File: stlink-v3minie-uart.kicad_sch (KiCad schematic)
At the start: 0 parts

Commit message: schem: add all connectors
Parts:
- added J1: Conn_02x05_Top_Bottom, GLCS:KYOCERA_AVX9159-006, symbol Connector_Generic:Conn_02x05_Top_Bottom
- added J2: Conn_01x04_Pin, Connector_PinHeader_2.54mm:PinHeader_1x04_P2.54mm_Vertical, symbol Connector:Conn_01x04_Pin
- added J3: Conn_01x05, symbol Connector_Generic:Conn_01x05
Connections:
- new net +3V3: J1.10 (Pin_10), J2.1 (Pin_1)
- new net GND: J1.6 (Pin_6), J2.3 (Pin_3)
- new net JTDI: J1.2 (Pin_2), J3.4 (Pin_4)
- new net SWCLK: J1.4 (Pin_4), J3.2 (Pin_2)
- new net SWDIO: J1.3 (Pin_3), J3.3 (Pin_3)
- new net SWO: J1.5 (Pin_5), J3.1 (Pin_1)
- new net VCP_RX: J1.7 (Pin_7), J2.4 (Pin_4)
- new net VCP_TX: J1.8 (Pin_8), J2.2 (Pin_2)
- new net nRST: J1.9 (Pin_9), J3.5 (Pin_5)
- no-connect marks 0 -> 1
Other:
- note added: "Breakout"
- note added: "STLINK-V3MINIE B2B edge connector"
- note added: "UART"

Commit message: schem: assign footprints
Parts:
- J3: footprint (none) -> Connector_PinHeader_2.54mm:PinHeader_1x05_P2.54mm_Horizontal
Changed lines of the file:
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@@
 			)
 		)
-		(property "Footprint" ""
+		(property "Footprint" "Connector_PinHeader_2.54mm:PinHeader_1x05_P2.54mm_Horizontal"
 			(at 105.41 104.14 0)
 			(hide yes)

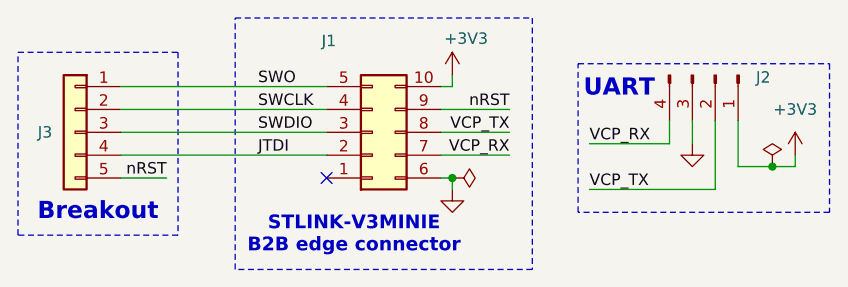
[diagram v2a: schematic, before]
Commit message: schem: renumber
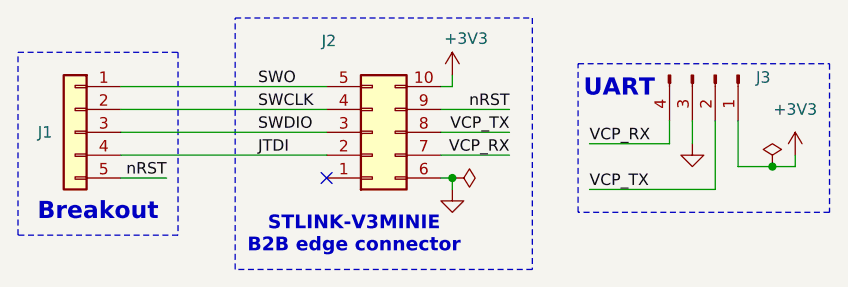
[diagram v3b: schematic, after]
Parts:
- renumbered J3 to J1, J1 to J2, J2 to J3
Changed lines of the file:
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@@
 		(in_pos_files yes)
 		(dnp no)
-		(property "Reference" "J1"
+		(property "Reference" "J2"
 			(at 133.604 93.98 0)
 			(show_name no)
@@
 			(project "stlink-v3minie-uart"
 				(path "/efe53425-0bb8-4b47-9e35-dff4b195a83f"
-					(reference "J1")
+					(reference "J2")
 					(unit 1)
 				)
@@
 		(dnp no)
 		(fields_autoplaced yes)
-		(property "Reference" "#FLG01"
+		(property "Reference" "#FLG02"
 			(at 182.88 106.045 0)
 			(hide yes)
@@
 			(project "stlink-v3minie-uart"
 				(path "/efe53425-0bb8-4b47-9e35-dff4b195a83f"
-					(reference "#FLG01")
+					(reference "#FLG02")
 					(unit 1)
 				)
@@
 		(dnp no)
 		(fields_autoplaced yes)
-		(property "Reference" "#PWR08"
+		(property "Reference" "#PWR04"
 			(at 185.42 110.49 0)
 			(hide yes)
@@
 			(project "stlink-v3minie-uart"
 				(path "/efe53425-0bb8-4b47-9e35-dff4b195a83f"
-					(reference "#PWR08")
+					(reference "#PWR04")
 					(unit 1)
 				)
@@
 		(dnp no)
 		(fields_autoplaced yes)
-		(property "Reference" "J3"
+		(property "Reference" "J1"
 			(at 102.87 104.1399 0)
 			(show_name no)
@@
 			(project "stlink-v3minie-uart"
 				(path "/efe53425-0bb8-4b47-9e35-dff4b195a83f"
-					(reference "J3")
+					(reference "J1")
 					(unit 1)
 				)
@@
 		(in_pos_files yes)
 		(dnp no)
-		(property "Reference" "#PWR011"
+		(property "Reference" "#PWR01"
 			(at 147.32 101.6 0)
 			(hide yes)
@@
 			(project "stlink-v3minie-uart"
 				(path "/efe53425-0bb8-4b47-9e35-dff4b195a83f"
-					(reference "#PWR011")
+					(reference "#PWR01")
 					(unit 1)
 				)
@@
 		(in_pos_files yes)
 		(dnp no)
-		(property "Reference" "#PWR09"
+		(property "Reference" "#PWR03"
 			(at 173.99 111.76 0)
 			(hide yes)
@@
 			(project "stlink-v3minie-uart"
 				(path "/efe53425-0bb8-4b47-9e35-dff4b195a83f"
-					(reference "#PWR09")
+					(reference "#PWR03")
 					(unit 1)
 				)
@@
 		(in_pos_files yes)
 		(dnp no)
-		(property "Reference" "#PWR010"
+		(property "Reference" "#PWR02"
 			(at 147.32 116.84 0)
 			(hide yes)
@@
 			(project "stlink-v3minie-uart"
 				(path "/efe53425-0bb8-4b47-9e35-dff4b195a83f"
-					(reference "#PWR010")
+					(reference "#PWR02")
 					(unit 1)
 				)
@@
 		(in_pos_files yes)
 		(dnp no)
-		(property "Reference" "J2"
+		(property "Reference" "J3"
 			(at 181.864 98.044 90)
 			(show_name no)
@@
 			(project "stlink-v3minie-uart"
 				(path "/efe53425-0bb8-4b47-9e35-dff4b195a83f"
-					(reference "J2")
+					(reference "J3")
 					(unit 1)
 				)
@@
 		(dnp no)
 		(fields_autoplaced yes)
-		(property "Reference" "#FLG02"
+		(property "Reference" "#FLG01"
 			(at 149.225 109.22 0)
 			(hide yes)
@@
 			(project "stlink-v3minie-uart"
 				(path "/efe53425-0bb8-4b47-9e35-dff4b195a83f"
-					(reference "#FLG02")
-					(unit 1)
-				)
+					(reference "#FLG01")
+					(unit 1)
+				)

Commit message: schem: add title
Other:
- company: (none) -> Rémi Ait-Younes
- title: (none) -> STLINK-V3 MINIE UART
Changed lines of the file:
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@@
 	(generator_version "10.0")
 	(paper "A4")
+	(title_block
+		(title "STLINK-V3 MINIE UART")
+		(date "2026-05-26")
+		(rev "01")
+		(company "Rémi Ait-Younes")
+	)
 	(rectangle
 		(start 99.06 95.25)

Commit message: pcb: initial rough placement
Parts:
- J1: footprint Connector_PinHeader_2.54mm:PinHeader_1x05_P2.54mm_Horizontal -> Connector_PinHeader_2.54mm:PinHeader_1x05_P2.54mm_Vertical
- J3: footprint Connector_PinHeader_2.54mm:PinHeader_1x04_P2.54mm_Vertical -> Connector_PinHeader_2.54mm:PinHeader_1x04_P2.54mm_Horizontal
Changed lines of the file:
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@@
 			)
 		)
-		(property "Footprint" "Connector_PinHeader_2.54mm:PinHeader_1x05_P2.54mm_Horizontal"
+		(property "Footprint" "Connector_PinHeader_2.54mm:PinHeader_1x05_P2.54mm_Vertical"
 			(at 105.41 104.14 0)
 			(hide yes)
@@
 			)
 		)
-		(property "Footprint" "Connector_PinHeader_2.54mm:PinHeader_1x04_P2.54mm_Vertical"
+		(property "Footprint" "Connector_PinHeader_2.54mm:PinHeader_1x04_P2.54mm_Horizontal"
 			(at 176.53 97.79 0)
 			(hide yes)
